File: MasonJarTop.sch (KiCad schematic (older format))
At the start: 14 parts, among them P1 CONN_01X02, P2 Loop Mounting Hole, P3 Loop Mounting Hole

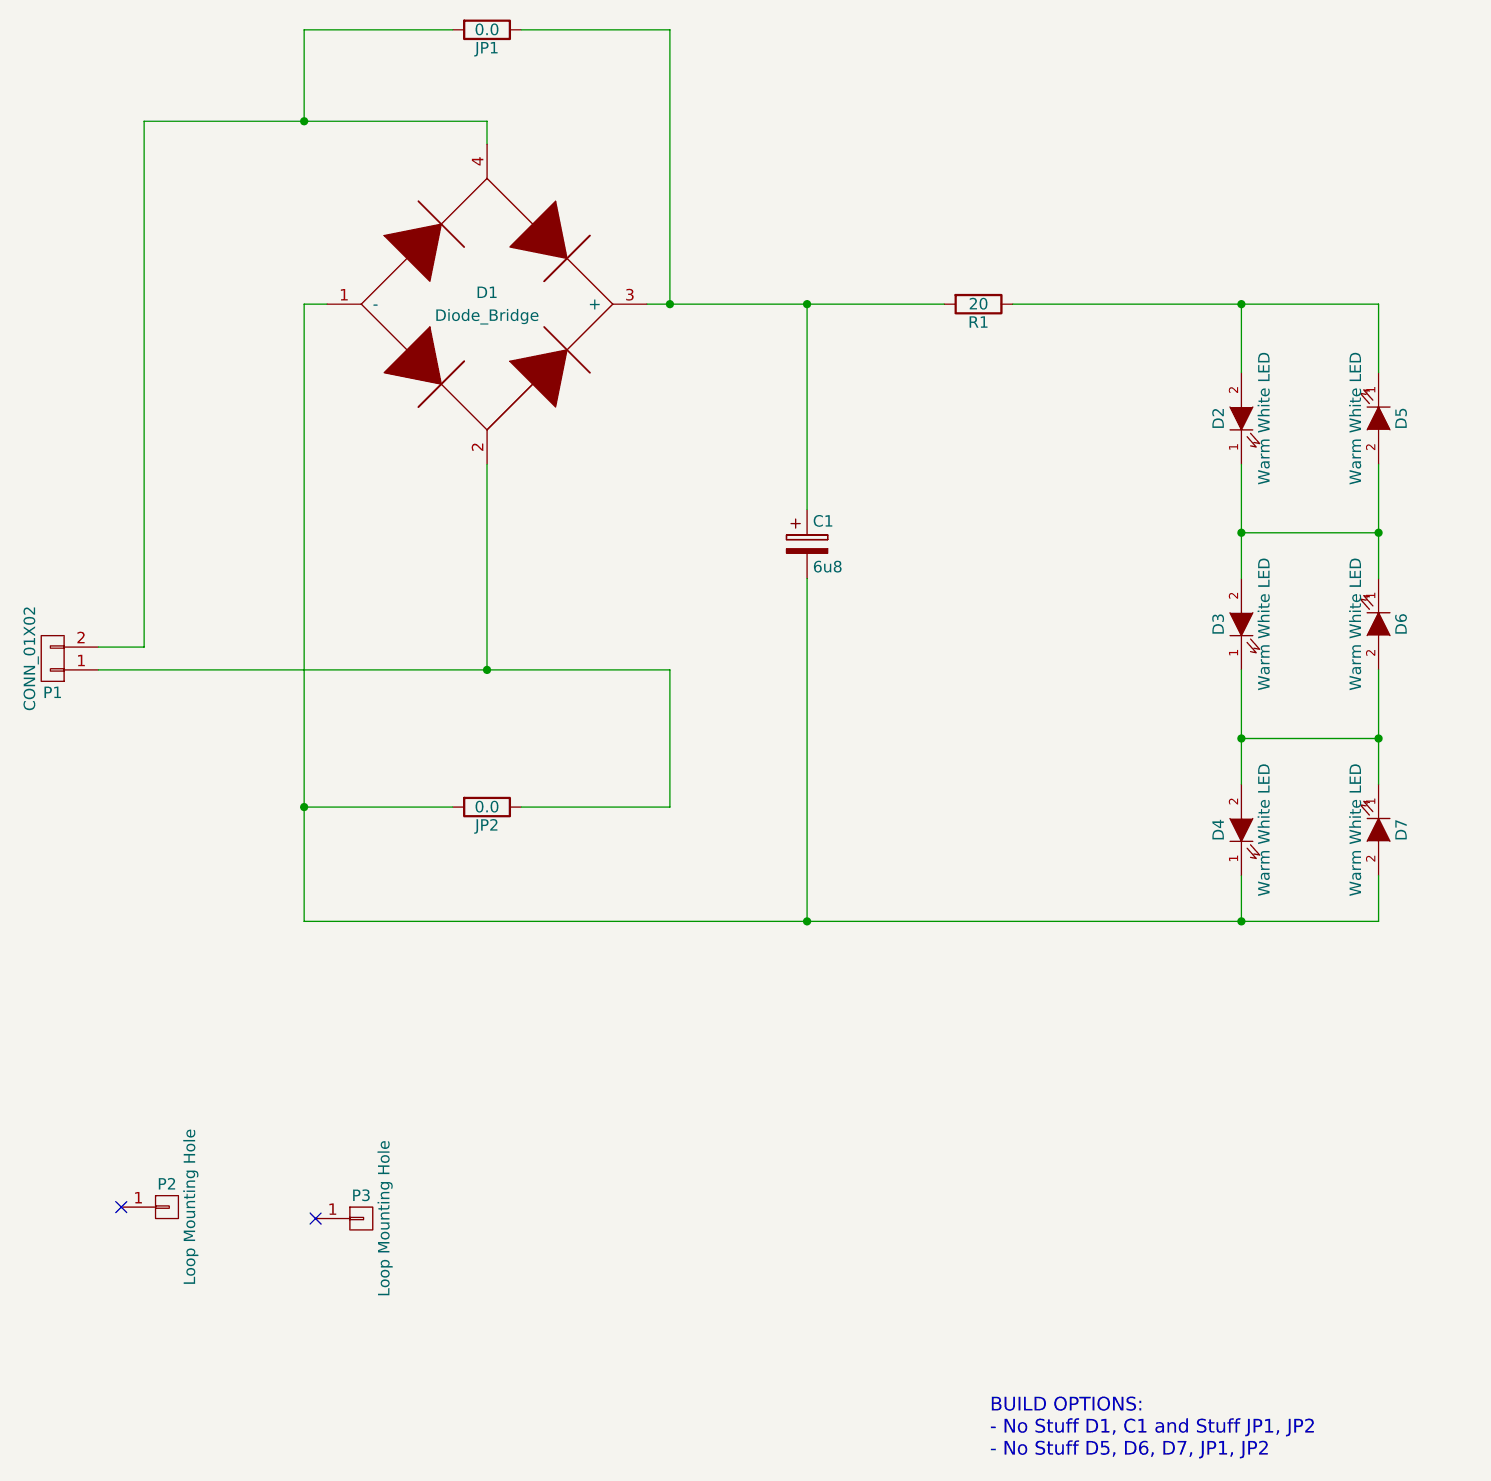
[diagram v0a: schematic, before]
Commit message: Updating schematic to use discrete diodes.
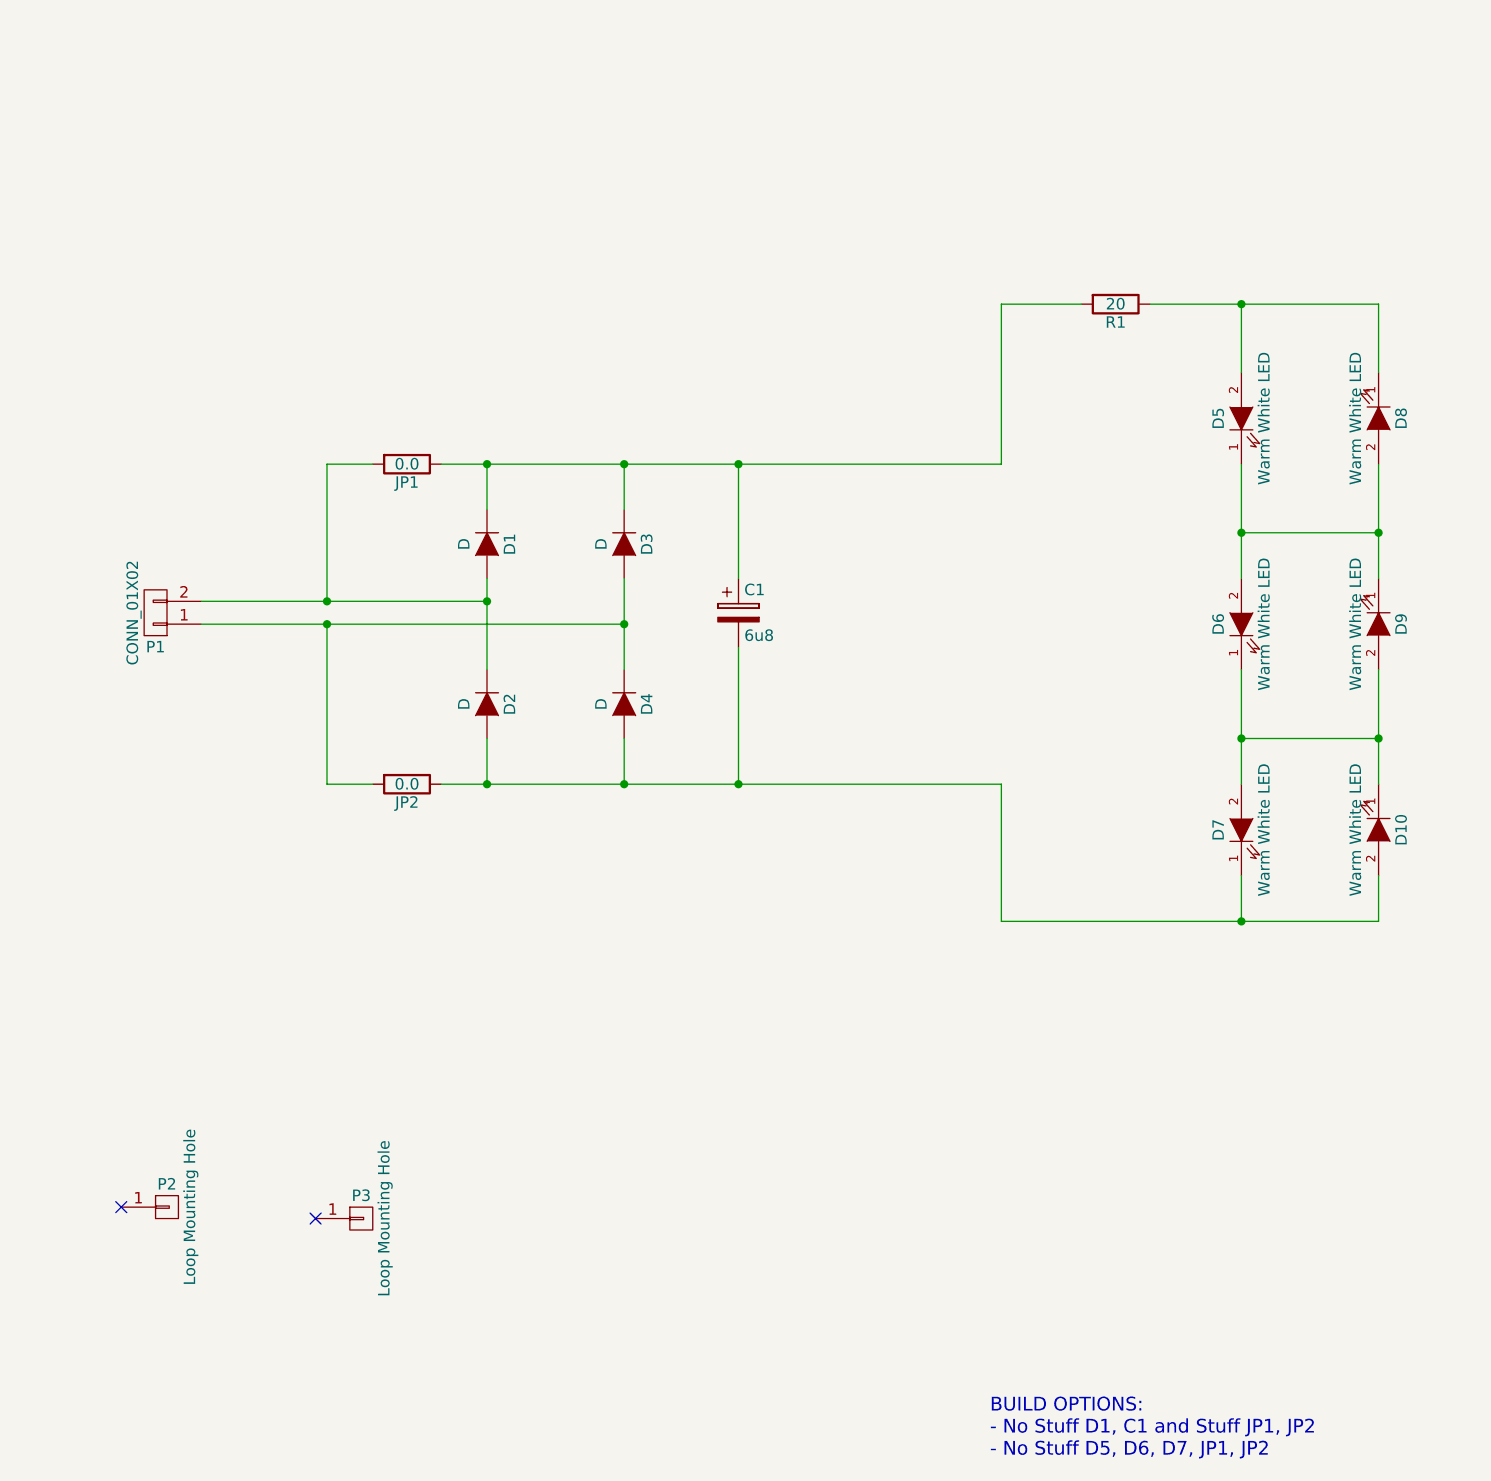
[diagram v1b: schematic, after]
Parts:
- removed D1: Diode_Bridge, symbol Diode_Bridge
- added D1, D2, D3, D4: D, Diodes_SMD:SOD-123, symbol D
- C1: footprint Capacitors_Tantalum_SMD:TantalC_SizeC_EIA-6032_HandSoldering -> Capacitors_SMD:c_elec_4x5.3
- D10: renamed from D7; footprint Resistors_SMD:R_1206_HandSoldering -> LEDs:LED_1206
- D5: renamed from D2; footprint Resistors_SMD:R_1206_HandSoldering -> LEDs:LED_1206
- D6: renamed from D3; footprint Resistors_SMD:R_1206_HandSoldering -> LEDs:LED_1206
- D7: renamed from D4; footprint Resistors_SMD:R_1206_HandSoldering -> LEDs:LED_1206
- D8: renamed from D5; footprint Resistors_SMD:R_1206_HandSoldering -> LEDs:LED_1206
- D9: renamed from D6; footprint Resistors_SMD:R_1206_HandSoldering -> LEDs:LED_1206
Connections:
- net at C1.2, D10.2 (A), D7.1 (K): now also JP2.1, D2.2 (A), D4.2 (A); no longer JP2.2
- net at P1.1 (P1): now also JP2.2, D3.2 (A), D4.1 (K); no longer JP2.1
- net at C1.1, JP1.1, R1.2: now also D1.1 (K), D3.1 (K)
- net at JP1.2, P1.2 (P2): now also D1.2 (A), D2.1 (K)
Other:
- moved on the sheet: C1, JP1, JP2, P1, R1
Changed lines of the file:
@@
 EESchema Schematic File Version 2
+LIBS:MasonJarTop-rescue
 LIBS:power
 LIBS:device
@@
 $EndDescr
 $Comp
-L Diode_Bridge D1
-U 1 1 576C2DDD
-P 4100 2300
-F 0 "D1" H 4100 2350 50  0000 C CNN
-F 1 "Diode_Bridge" H 4100 2250 50  0000 C CNN
-F 2 "" H 4100 2300 60  0001 C CNN
-F 3 "" H 4100 2300 60  0000 C CNN
-F 4 "MB8SCT-ND" H 4100 2300 60  0001 C CNN "DigiKey"
-	1    4100 2300
-	1    0    0    -1
-$EndComp
-$Comp
-L LED D2
+L LED D5
 U 1 1 576C2FA9
 P 7400 2800
-F 0 "D2" H 7400 2900 50  0000 C CNN
+F 0 "D5" H 7400 2900 50  0000 C CNN
 F 1 "Warm White LED" H 7400 2700 50  0000 C CNN
-F 2 "Resistors_SMD:R_1206_HandSoldering" H 7400 2800 60  0001 C CNN
+F 2 "LEDs:LED_1206" H 7400 2800 60  0001 C CNN
 F 3 "" H 7400 2800 60  0000 C CNN
 F 4 "1416-1216-1-ND" H 7400 2800 60  0001 C CNN "DigiKey"
@@
 $EndComp
 $Comp
-L LED D3
+L LED D6
 U 1 1 576C3263
 P 7400 3700
-F 0 "D3" H 7400 3800 50  0000 C CNN
+F 0 "D6" H 7400 3800 50  0000 C CNN
 F 1 "Warm White LED" H 7400 3600 50  0000 C CNN
-F 2 "Resistors_SMD:R_1206_HandSoldering" H 7400 3700 60  0001 C CNN
+F 2 "LEDs:LED_1206" H 7400 3700 60  0001 C CNN
 F 3 "" H 7400 3700 60  0000 C CNN
 F 4 "1416-1216-1-ND" H 7400 3700 60  0001 C CNN "DigiKey"
@@
 $EndComp
 $Comp
-L LED D4
+L LED D7
 U 1 1 576C32AA
 P 7400 4600
-F 0 "D4" H 7400 4700 50  0000 C CNN
+F 0 "D7" H 7400 4700 50  0000 C CNN
 F 1 "Warm White LED" H 7400 4500 50  0000 C CNN
-F 2 "Resistors_SMD:R_1206_HandSoldering" H 7400 4600 60  0001 C CNN
+F 2 "LEDs:LED_1206" H 7400 4600 60  0001 C CNN
 F 3 "" H 7400 4600 60  0000 C CNN
 F 4 "1416-1216-1-ND" H 7400 4600 60  0001 C CNN "DigiKey"
@@
 L CONN_01X02 P1
 U 1 1 576C33A1
-P 2200 3850
-F 0 "P1" H 2200 4000 50  0000 C CNN
-F 1 "CONN_01X02" V 2300 3850 50  0000 C CNN
-F 2 "Wire_Pads:SolderWirePad_2x_1-2mmDrill" H 2200 3850 60  0001 C CNN
-F 3 "" H 2200 3850 60  0000 C CNN
-	1    2200 3850
+P 2650 3650
+F 0 "P1" H 2650 3800 50  0000 C CNN
+F 1 "CONN_01X02" V 2750 3650 50  0000 C CNN
+F 2 "Wire_Pads:SolderWirePad_2x_1-2mmDrill" H 2650 3650 60  0001 C CNN
+F 3 "" H 2650 3650 60  0000 C CNN
+	1    2650 3650
 	-1   0    0    1
 $EndComp
@@
 L R R1
 U 1 1 576C34CD
-P 6250 2300
-F 0 "R1" V 6330 2300 50  0000 C CNN
-F 1 "20" V 6250 2300 50  0000 C CNN
-F 2 "Resistors_SMD:R_1206_HandSoldering" V 6180 2300 30  0001 C CNN
-F 3 "" H 6250 2300 30  0000 C CNN
-F 4 "311-20ERCT-ND" V 6250 2300 60  0001 C CNN "DigiKey"
-	1    6250 2300
+P 6850 2300
+F 0 "R1" V 6930 2300 50  0000 C CNN
+F 1 "20" V 6850 2300 50  0000 C CNN
+F 2 "Resistors_SMD:R_1206_HandSoldering" V 6780 2300 30  0001 C CNN
+F 3 "" H 6850 2300 30  0000 C CNN
+F 4 "311-20ERCT-ND" V 6850 2300 60  0001 C CNN "DigiKey"
+	1    6850 2300
 	0    1    1    0
 $EndComp
@@
 L CP C1
 U 1 1 576C359C
-P 5500 3350
-F 0 "C1" H 5525 3450 50  0000 L CNN
-F 1 "6u8" H 5525 3250 50  0000 L CNN
-F 2 "Capacitors_Tantalum_SMD:TantalC_SizeC_EIA-6032_HandSoldering" H 5538 3200 30  0001 C CNN
-F 3 "" H 5500 3350 60  0000 C CNN
-F 4 "732-8429-1-ND" H 5500 3350 60  0001 C CNN "DigiKey"
-	1    5500 3350
+P 5200 3650
+F 0 "C1" H 5225 3750 50  0000 L CNN
+F 1 "6u8" H 5225 3550 50  0000 L CNN
+F 2 "Capacitors_SMD:c_elec_4x5.3" H 5238 3500 30  0001 C CNN
+F 3 "" H 5200 3650 60  0000 C CNN
+F 4 "732-8429-1-ND" H 5200 3650 60  0001 C CNN "DigiKey"
+	1    5200 3650
 	1    0    0    -1
 $EndComp
 NoConn ~ 3350 6300
 NoConn ~ 2500 6250
-Wire Wire Line
-	2400 3800 2600 3800
-Wire Wire Line
-	2600 3800 2600 1500
-Wire Wire Line
-	2600 1500 4100 1500
-Wire Wire Line
-	4100 1500 4100 1600
-Wire Wire Line
-	2400 3900 4900 3900
-Wire Wire Line
-	4100 3900 4100 3000
-Wire Wire Line
-	4800 2300 6100 2300
-Wire Wire Line
-	6400 2300 8000 2300
-Wire Wire Line
-	7400 2300 7400 2600
-Wire Wire Line
-	7400 3000 7400 3500
-Wire Wire Line
-	7400 3900 7400 4400
-Wire Wire Line
-	7400 4800 7400 5000
-Wire Wire Line
-	3300 5000 8000 5000
-Wire Wire Line
-	3300 2300 3400 2300
-Wire Wire Line
-	5500 3200 5500 2300
-Connection ~ 5500 2300
-Wire Wire Line
-	5500 3500 5500 5000
-Connection ~ 5500 5000
-$Comp
-L LED D5
+$Comp
+L LED D8
 U 1 1 576D6D77
 P 8000 2800
-F 0 "D5" H 8000 2900 50  0000 C CNN
+F 0 "D8" H 8000 2900 50  0000 C CNN
 F 1 "Warm White LED" H 8000 2700 50  0000 C CNN
-F 2 "Resistors_SMD:R_1206_HandSoldering" H 8000 2800 60  0001 C CNN
+F 2 "LEDs:LED_1206" H 8000 2800 60  0001 C CNN
 F 3 "" H 8000 2800 60  0000 C CNN
 F 4 "1416-1216-1-ND" H 8000 2800 60  0001 C CNN "DigiKey"
@@
 $EndComp
 $Comp
-L LED D6
+L LED D9
 U 1 1 576D6DBF
 P 8000 3700
-F 0 "D6" H 8000 3800 50  0000 C CNN
+F 0 "D9" H 8000 3800 50  0000 C CNN
 F 1 "Warm White LED" H 8000 3600 50  0000 C CNN
-F 2 "Resistors_SMD:R_1206_HandSoldering" H 8000 3700 60  0001 C CNN
+F 2 "LEDs:LED_1206" H 8000 3700 60  0001 C CNN
 F 3 "" H 8000 3700 60  0000 C CNN
 F 4 "1416-1216-1-ND" H 8000 3700 60  0001 C CNN "DigiKey"
@@
 $EndComp
 $Comp
-L LED D7
+L LED D10
 U 1 1 576D6E06
 P 8000 4600
-F 0 "D7" H 8000 4700 50  0000 C CNN
+F 0 "D10" H 8000 4700 50  0000 C CNN
 F 1 "Warm White LED" H 8000 4500 50  0000 C CNN
-F 2 "Resistors_SMD:R_1206_HandSoldering" H 8000 4600 60  0001 C CNN
+F 2 "LEDs:LED_1206" H 8000 4600 60  0001 C CNN
 F 3 "" H 8000 4600 60  0000 C CNN
 F 4 "1416-1216-1-ND" H 8000 4600 60  0001 C CNN "DigiKey"
@@
 	0    1    1    0
 $EndComp
+Text Notes 6300 7350 0    60   ~ 0
+BUILD OPTIONS:\n- No Stuff D1, C1 and Stuff JP1, JP2\n- No Stuff D5, D6, D7, JP1, JP2
+$Comp
+L R JP1
+U 1 1 576D7B6C
+P 3750 3000
+F 0 "JP1" V 3830 3000 50  0000 C CNN
+F 1 "0.0" V 3750 3000 50  0000 C CNN
+F 2 "Resistors_SMD:R_1206_HandSoldering" V 3680 3000 30  0001 C CNN
+F 3 "" H 3750 3000 30  0000 C CNN
+F 4 "311-20ERCT-ND" V 3750 3000 60  0001 C CNN "DigiKey"
+	1    3750 3000
+	0    1    1    0
+$EndComp
+$Comp
+L R JP2
+U 1 1 576D7BEA
+P 3750 4400
+F 0 "JP2" V 3830 4400 50  0000 C CNN
+F 1 "0.0" V 3750 4400 50  0000 C CNN
+F 2 "Resistors_SMD:R_1206_HandSoldering" V 3680 4400 30  0001 C CNN
+F 3 "" H 3750 4400 30  0000 C CNN
+F 4 "311-20ERCT-ND" V 3750 4400 60  0001 C CNN "DigiKey"
+	1    3750 4400
+	0    1    1    0
+$EndComp
+$Comp
+L D D3
+U 1 1 576F5EC5
+P 4700 3350
+F 0 "D3" H 4700 3450 50  0000 C CNN
+F 1 "D" H 4700 3250 50  0000 C CNN
+F 2 "Diodes_SMD:SOD-123" H 4700 3350 50  0001 C CNN
+F 3 "" H 4700 3350 50  0000 C CNN
+F 4 "DA2JF2300LCT-ND" H 4700 3350 60  0001 C CNN "DigiKey"
+	1    4700 3350
+	0    1    1    0
+$EndComp
+$Comp
+L D D1
+U 1 1 576F5F32
+P 4100 3350
+F 0 "D1" H 4100 3450 50  0000 C CNN
+F 1 "D" H 4100 3250 50  0000 C CNN
+F 2 "Diodes_SMD:SOD-123" H 4100 3350 50  0001 C CNN
+F 3 "" H 4100 3350 50  0000 C CNN
+F 4 "DA2JF2300LCT-ND" H 4100 3350 60  0001 C CNN "DigiKey"
+	1    4100 3350
+	0    1    1    0
+$EndComp
+$Comp
+L D D2
+U 1 1 576F5F89
+P 4100 4050
+F 0 "D2" H 4100 4150 50  0000 C CNN
+F 1 "D" H 4100 3950 50  0000 C CNN
+F 2 "Diodes_SMD:SOD-123" H 4100 4050 50  0001 C CNN
+F 3 "" H 4100 4050 50  0000 C CNN
+F 4 "DA2JF2300LCT-ND" H 4100 4050 60  0001 C CNN "DigiKey"
+	1    4100 4050
+	0    1    1    0
+$EndComp
+$Comp
+L D D4
+U 1 1 576F5FD9
+P 4700 4050
+F 0 "D4" H 4700 4150 50  0000 C CNN
+F 1 "D" H 4700 3950 50  0000 C CNN
+F 2 "Diodes_SMD:SOD-123" H 4700 4050 50  0001 C CNN
+F 3 "" H 4700 4050 50  0000 C CNN
+F 4 "DA2JF2300LCT-ND" H 4700 4050 60  0001 C CNN "DigiKey"
+	1    4700 4050
+	0    1    1    0
+$EndComp
+Wire Wire Line
+	7400 2300 7400 2600
+Wire Wire Line
+	7400 3000 7400 3500
+Wire Wire Line
+	7400 3900 7400 4400
+Wire Wire Line
+	7400 4800 7400 5000
 Wire Wire Line
 	8000 2300 8000 2600
-Connection ~ 7400 2300
 Wire Wire Line
 	8000 3000 8000 3500
@@
 Wire Wire Line
 	8000 5000 8000 4800
-Connection ~ 7400 5000
 Wire Wire Line
 	7400 4200 8000 4200
@@
 Connection ~ 7400 4200
 Wire Wire Line
-	3300 1100 3950 1100
-Wire Wire Line
-	4250 1100 4900 1100
-Wire Wire Line
-	4900 1100 4900 2300
-Connection ~ 4900 2300
-Wire Wire Line
-	3300 1100 3300 1500
-Connection ~ 3300 1500
-Wire Wire Line
-	3300 2300 3300 5000
-Wire Wire Line
-	3300 4500 3950 4500
-Connection ~ 3300 4500
-Wire Wire Line
-	4250 4500 4900 4500
-Wire Wire Line
-	4900 4500 4900 3900
-Connection ~ 4100 3900
-Text Notes 6300 7350 0    60   ~ 0
-BUILD OPTIONS:\n- No Stuff D1, C1 and Stuff JP1, JP2\n- No Stuff D5, D6, D7, JP1, JP2
-$Comp
-L R JP1
-U 1 1 576D7B6C
-P 4100 1100
-F 0 "JP1" V 4180 1100 50  0000 C CNN
-F 1 "0.0" V 4100 1100 50  0000 C CNN
-F 2 "Resistors_SMD:R_1206_HandSoldering" V 4030 1100 30  0001 C CNN
-F 3 "" H 4100 1100 30  0000 C CNN
-F 4 "311-20ERCT-ND" V 4100 1100 60  0001 C CNN "DigiKey"
-	1    4100 1100
-	0    1    1    0
-$EndComp
-$Comp
-L R JP2
-U 1 1 576D7BEA
-P 4100 4500
-F 0 "JP2" V 4180 4500 50  0000 C CNN
-F 1 "0.0" V 4100 4500 50  0000 C CNN
-F 2 "Resistors_SMD:R_1206_HandSoldering" V 4030 4500 30  0001 C CNN
-F 3 "" H 4100 4500 30  0000 C CNN
-F 4 "311-20ERCT-ND" V 4100 4500 60  0001 C CNN "DigiKey"
-	1    4100 4500
-	0    1    1    0
-$EndComp
+	4100 3900 4100 3500
+Wire Wire Line
+	4700 3900 4700 3500
+Wire Wire Line
+	2850 3600 4100 3600
+Connection ~ 4100 3600
+Wire Wire Line
+	2850 3700 4700 3700
+Connection ~ 4700 3700
+Wire Wire Line
+	3900 3000 6350 3000
+Wire Wire Line
+	4100 3000 4100 3200
+Wire Wire Line
+	4700 3000 4700 3200
+Connection ~ 4100 3000
+Wire Wire Line
+	3900 4400 6350 4400
+Wire Wire Line
+	4100 4400 4100 4200
+Wire Wire Line
+	4700 4400 4700 4200
+Connection ~ 4100 4400
+Wire Wire Line
+	3600 4400 3400 4400
+Wire Wire Line
+	3400 4400 3400 3700
+Connection ~ 3400 3700
+Wire Wire Line
+	3600 3000 3400 3000
+Wire Wire Line
+	3400 3000 3400 3600
+Connection ~ 3400 3600
+Wire Wire Line
+	5200 3000 5200 3500
+Connection ~ 4700 3000
+Wire Wire Line
+	5200 4400 5200 3800
+Connection ~ 4700 4400
+Wire Wire Line
+	7000 2300 8000 2300
+Connection ~ 7400 2300
+Wire Wire Line
+	6350 5000 8000 5000
+Wire Wire Line
+	6350 4400 6350 5000
+Connection ~ 5200 4400
+Connection ~ 7400 5000
+Wire Wire Line
+	6350 3000 6350 2300
+Wire Wire Line
+	6350 2300 6700 2300
+Connection ~ 5200 3000
 $EndSCHEMATC

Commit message: Layout done.
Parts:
- P1: footprint Wire_Pads:SolderWirePad_2x_1-2mmDrill -> Pin_Headers:Pin_Header_Straight_1x02
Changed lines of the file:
@@
 EESchema Schematic File Version 2
-LIBS:MasonJarTop-rescue
 LIBS:power
 LIBS:device
@@
 F 0 "P1" H 2650 3800 50  0000 C CNN
 F 1 "CONN_01X02" V 2750 3650 50  0000 C CNN
-F 2 "Wire_Pads:SolderWirePad_2x_1-2mmDrill" H 2650 3650 60  0001 C CNN
+F 2 "Pin_Headers:Pin_Header_Straight_1x02" H 2650 3650 60  0001 C CNN
 F 3 "" H 2650 3650 60  0000 C CNN
 	1    2650 3650
